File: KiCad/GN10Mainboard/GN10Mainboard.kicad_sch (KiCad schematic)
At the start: 130 parts, among them J1 USB_C_Receptacle_USB2.0_16P, J10 Conn_01x02_Pin, J2 Conn_01x04, J3 Conn_01x04, J4 USB_C_Receptacle_USB2.0_16P, J5 Conn_01x04, J6 Conn_01x06, J7 Conn_01x04, J8 Conn_01x04, J9 XT30PW-M, SW1 SW_DIP_x04, SW2 SW_Push, SW4 SW_Push, SW5 SW_Push, U1 STM32G474RCTx, U10 3.3V, U2 FT231XS, U3 RNBD451, U4 FT231XS, U5 MCP2562-E-SN, U6 MCP2562-E-SN, U7 BNO055, U8 7segmentLED, U9 OKL-T/x-W5N-C, Y1 32.768kHz, Y2 24MHz, Y3 Crystal

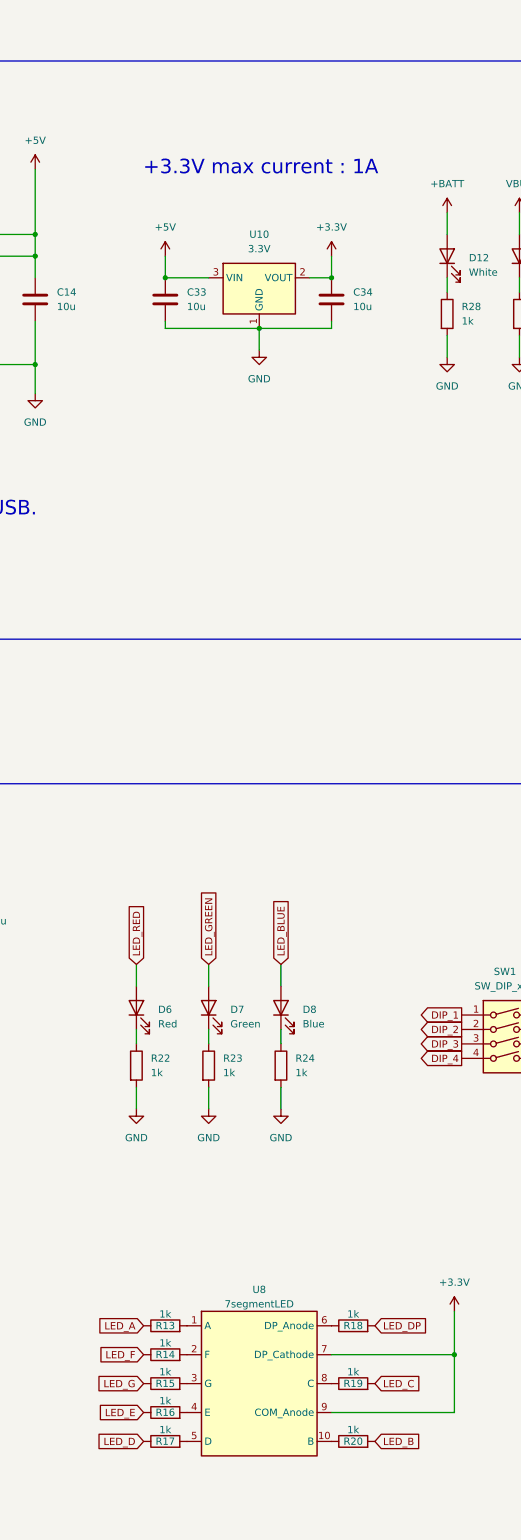
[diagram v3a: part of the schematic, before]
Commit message: Added a reverse voltage protection diode to the linear regulator and fixed the 7seg LED because its resistance was too high.
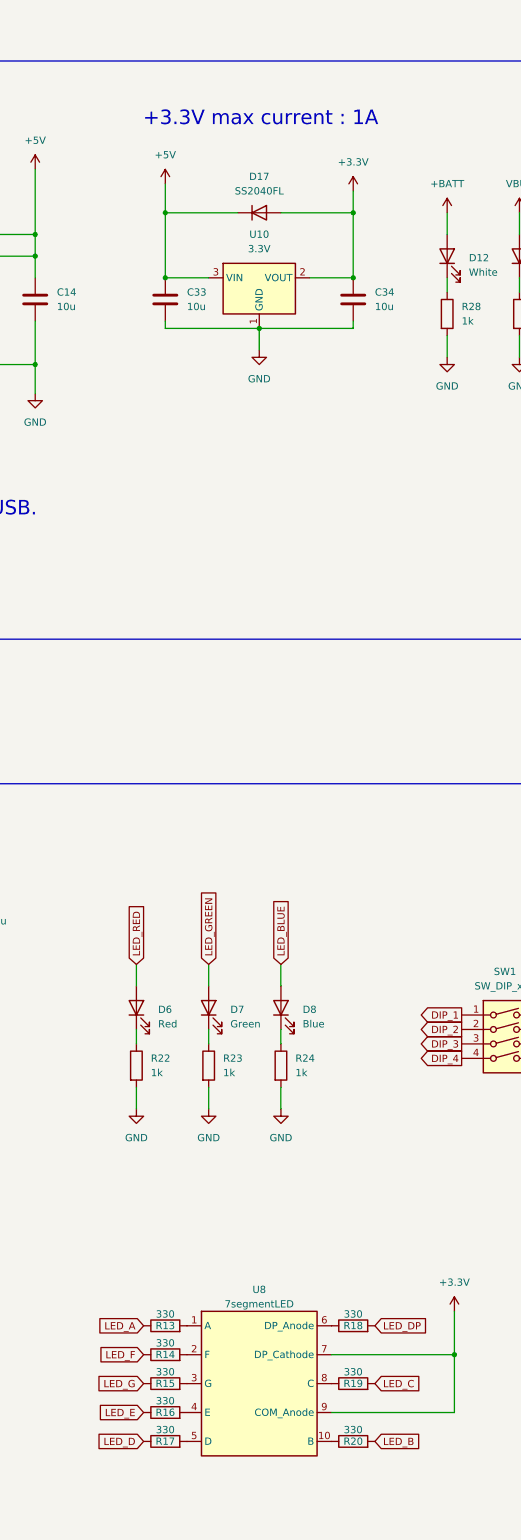
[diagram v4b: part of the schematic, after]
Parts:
- added D17: SS2040FL, symbol Device:D
- R13, R14, R15, R16, R17, R18, R19, R20: value 1k -> 330
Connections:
- net +3.3V: now also D17.2 (A)
- net +5V: now also D17.1 (K)
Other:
- moved on the sheet: C34
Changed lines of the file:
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@@
 	)
 	(junction
-		(at 203.2 63.5)
+		(at 207.01 63.5)
 		(diameter 0)
 		(color 0 0 0 0)
@@
 	)
 	(junction
+		(at 173.99 52.07)
+		(diameter 0)
+		(color 0 0 0 0)
+	)
+	(junction
 		(at 118.11 179.07)
 		(diameter 0)
@@
 		(color 0 0 0 0)
 	)
+	(junction
+		(at 207.01 52.07)
+		(diameter 0)
+		(color 0 0 0 0)
+	)
 	(no_connect
 		(at 431.8 77.47)
@@
 	(wire
 		(pts
-			(xy 203.2 71.12) (xy 203.2 72.39)
+			(xy 207.01 71.12) (xy 207.01 72.39)
 		)
 		(stroke
@@
 	(wire
 		(pts
+			(xy 173.99 52.07) (xy 186.69 52.07)
+		)
+		(stroke
+			(width 0)
+			(type default)
+		)
+	)
+	(wire
+		(pts
 			(xy 81.28 367.03) (xy 95.25 367.03)
 		)
@@
 	(wire
 		(pts
-			(xy 199.39 63.5) (xy 203.2 63.5)
+			(xy 199.39 63.5) (xy 207.01 63.5)
 		)
 		(stroke
@@
 	(wire
 		(pts
-			(xy 173.99 59.69) (xy 173.99 63.5)
+			(xy 173.99 46.99) (xy 173.99 52.07)
 		)
 		(stroke
@@
 	(wire
 		(pts
+			(xy 173.99 52.07) (xy 173.99 63.5)
+		)
+		(stroke
+			(width 0)
+			(type default)
+		)
+	)
+	(wire
+		(pts
 			(xy 455.93 82.55) (xy 448.31 82.55)
 		)
@@
 	(wire
 		(pts
+			(xy 194.31 52.07) (xy 207.01 52.07)
+		)
+		(stroke
+			(width 0)
+			(type default)
+		)
+	)
+	(wire
+		(pts
 			(xy 67.31 198.12) (xy 67.31 200.66)
 		)
@@
 	(wire
 		(pts
+			(xy 207.01 52.07) (xy 207.01 63.5)
+		)
+		(stroke
+			(width 0)
+			(type default)
+		)
+	)
+	(wire
+		(pts
 			(xy 345.44 377.19) (xy 358.14 377.19)
 		)
@@
 	(wire
 		(pts
-			(xy 203.2 72.39) (xy 190.5 72.39)
+			(xy 207.01 72.39) (xy 190.5 72.39)
 		)
 		(stroke
@@
 	(wire
 		(pts
-			(xy 203.2 59.69) (xy 203.2 63.5)
+			(xy 207.01 48.26) (xy 207.01 52.07)
 		)
 		(stroke
@@
 	(text "+3.3V max current : 1A"
 		(exclude_from_sim no)
-		(at 190.754 44.196 0)
+		(at 190.754 35.56 0)
 		(effects
 			(font
@@
 			)
 		)
-		(property "Value" "1k"
+		(property "Value" "330"
 			(at 207.01 265.938 90)
 			(effects
@@
 			)
 		)
-		(property "Value" "1k"
+		(property "Value" "330"
 			(at 173.99 245.618 90)
 			(effects
@@
 			)
 		)
-		(property "Value" "1k"
+		(property "Value" "330"
 			(at 173.99 250.698 90)
 			(effects
@@
 			)
 		)
-		(property "Value" "1k"
+		(property "Value" "330"
 			(at 173.99 265.938 90)
 			(effects
@@
 			)
 		)
-		(property "Value" "1k"
+		(property "Value" "330"
 			(at 173.99 255.778 90)
 			(effects
@@
 			)
 		)
-		(property "Value" "1k"
+		(property "Value" "330"
 			(at 207.01 245.618 90)
 			(effects
@@
 	(symbol
 		(lib_id "Device:C")
-		(at 203.2 67.31 0)
+		(at 207.01 67.31 0)
 		(unit 1)
 		(exclude_from_sim no)
@@
 		(fields_autoplaced yes)
 		(property "Reference" "C34"
-			(at 207.01 66.0399 0)
+			(at 210.82 66.0399 0)
 			(effects
 				(font
@@
 		)
 		(property "Value" "10u"
-			(at 207.01 68.5799 0)
+			(at 210.82 68.5799 0)
 			(effects
 				(font
@@
 		)
 		(property "Footprint" ""
-			(at 204.1652 71.12 0)
+			(at 207.9752 71.12 0)
 			(effects
 				(font
@@
 		)
 		(property "Datasheet" "~"
-			(at 203.2 67.31 0)
+			(at 207.01 67.31 0)
 			(effects
 				(font
@@
 		)
 		(property "Description" "Unpolarized capacitor"
-			(at 203.2 67.31 0)
+			(at 207.01 67.31 0)
 			(effects
 				(font
@@
 			)
 		)
-		(property "Value" "1k"
+		(property "Value" "330"
 			(at 173.99 260.858 90)
 			(effects
@@
 	)
 	(symbol
+		(lib_id "Device:D")
+		(at 190.5 52.07 0)
+		(unit 1)
+		(exclude_from_sim no)
+		(in_bom yes)
+		(on_board yes)
+		(dnp no)
+		(fields_autoplaced yes)
+		(property "Reference" "D17"
+			(at 190.5 45.72 0)
+			(effects
+				(font
+					(size 1.27 1.27)
+				)
+			)
+		)
+		(property "Value" "SS2040FL"
+			(at 190.5 48.26 0)
+			(effects
+				(font
+					(size 1.27 1.27)
+				)
+			)
+		)
+		(property "Footprint" ""
+			(at 190.5 52.07 0)
+			(effects
+				(font
+					(size 1.27 1.27)
+				)
+				(hide yes)
+			)
+		)
+		(property "Datasheet" "~"
+			(at 190.5 52.07 0)
+			(effects
+				(font
+					(size 1.27 1.27)
+				)
+				(hide yes)
+			)
+		)
+		(property "Description" "Diode"
+			(at 190.5 52.07 0)
+			(effects
+				(font
+					(size 1.27 1.27)
+				)
+				(hide yes)
+			)
+		)
+		(property "Sim.Device" "D"
+			(at 190.5 52.07 0)
+			(effects
+				(font
+					(size 1.27 1.27)
+				)
+				(hide yes)
+			)
+		)
+		(property "Sim.Pins" "1=K 2=A"
+			(at 190.5 52.07 0)
+			(effects
+				(font
+					(size 1.27 1.27)
+				)
+				(hide yes)
+			)
+		)
+		(pin "1"
+		)
+		(pin "2"
+		)
+		(instances
+			(project ""
+				(path "/b58ae320-37f1-47e7-bf16-145390e42e75"
+					(reference "D17")
+					(unit 1)
+				)
+			)
+		)
+	)
+	(symbol
 		(lib_id "power:GND")
 		(at 142.24 242.57 0)
@@
 	(symbol
 		(lib_id "power:+3.3V")
-		(at 203.2 59.69 0)
+		(at 207.01 48.26 0)
 		(unit 1)
 		(exclude_from_sim no)
@@
 		(fields_autoplaced yes)
 		(property "Reference" "#PWR069"
-			(at 203.2 63.5 0)
+			(at 207.01 52.07 0)
 			(effects
 				(font
@@
 		)
 		(property "Value" "+3.3V"
-			(at 203.2 54.61 0)
+			(at 207.01 43.18 0)
 			(effects
 				(font
@@
 		)
 		(property "Footprint" ""
-			(at 203.2 59.69 0)
+			(at 207.01 48.26 0)
 			(effects
 				(font
@@
 		)
 		(property "Datasheet" ""
-			(at 203.2 59.69 0)
+			(at 207.01 48.26 0)
 			(effects
 				(font
@@
 		)
 		(property "Description" "Power symbol creates a global label with name \"+3.3V\""
-			(at 203.2 59.69 0)
+			(at 207.01 48.26 0)
 			(effects
 				(font
@@
 	(symbol
 		(lib_id "power:+5V")
-		(at 173.99 59.69 0)
+		(at 173.99 46.99 0)
 		(unit 1)
 		(exclude_from_sim no)
@@
 		(fields_autoplaced yes)
 		(property "Reference" "#PWR067"
-			(at 173.99 63.5 0)
+			(at 173.99 50.8 0)
 			(effects
 				(font
@@
 		)
 		(property "Value" "+5V"
-			(at 173.99 54.61 0)
+			(at 173.99 41.91 0)
 			(effects
 				(font
@@
 		)
 		(property "Footprint" ""
-			(at 173.99 59.69 0)
+			(at 173.99 46.99 0)
 			(effects
 				(font
@@
 		)
 		(property "Datasheet" ""
-			(at 173.99 59.69 0)
+			(at 173.99 46.99 0)
 			(effects
 				(font
@@
 		)
 		(property "Description" "Power symbol creates a global label with name \"+5V\""
-			(at 173.99 59.69 0)
+			(at 173.99 46.99 0)
 			(effects
 				(font
@@
 			)
 		)
-		(property "Value" "1k"
+		(property "Value" "330"
 			(at 207.01 255.778 90)
 			(effects

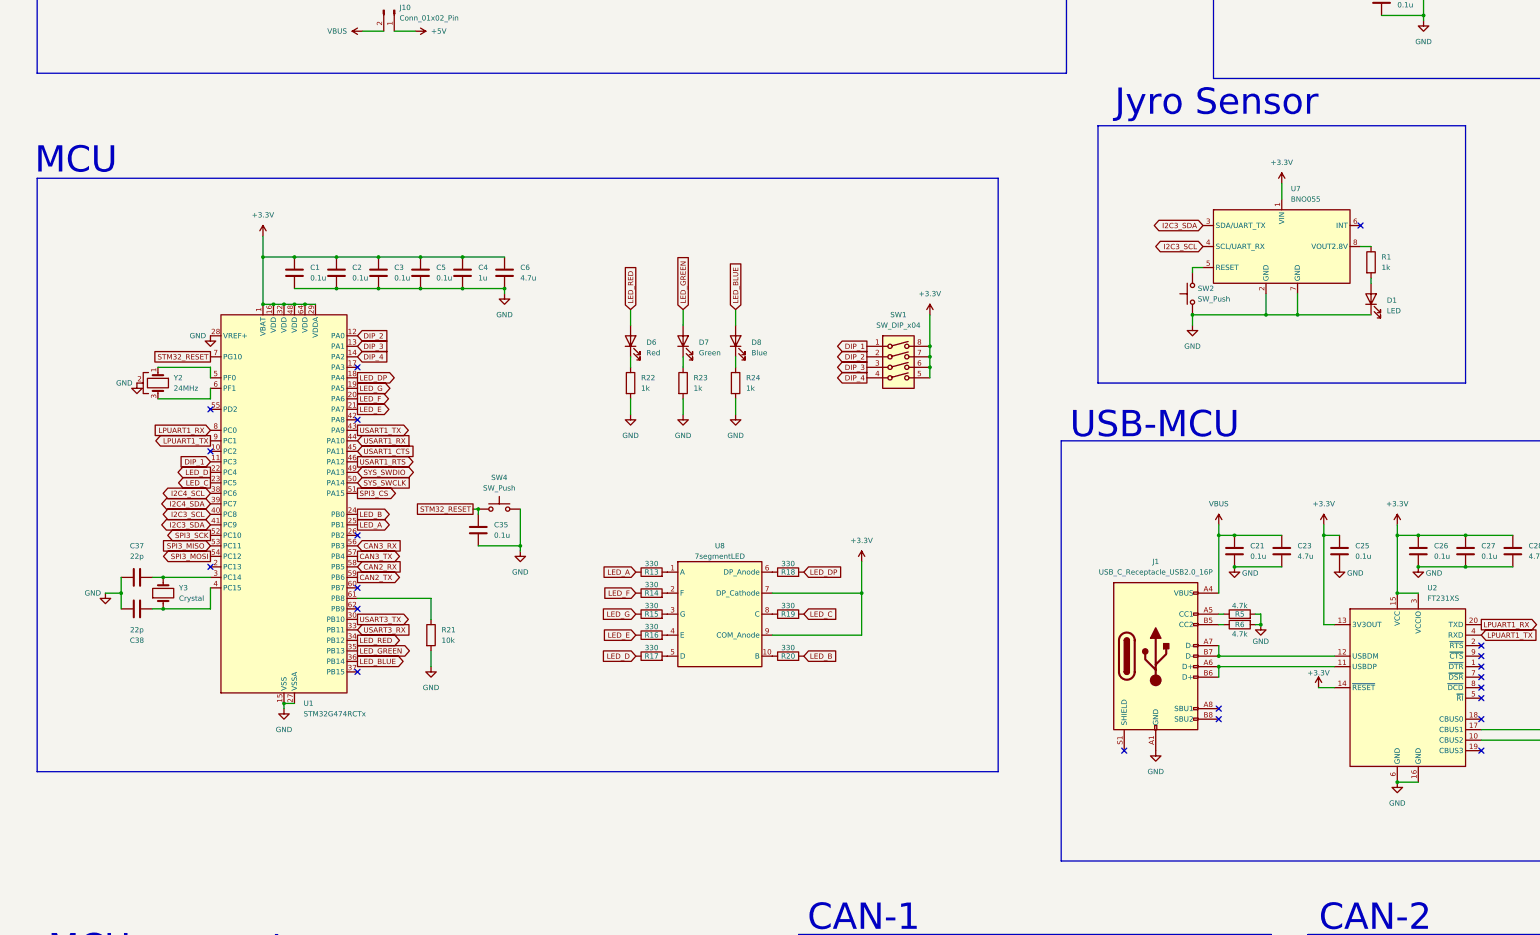
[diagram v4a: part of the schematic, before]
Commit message: add: transistor array for drive a 7 segment LED.
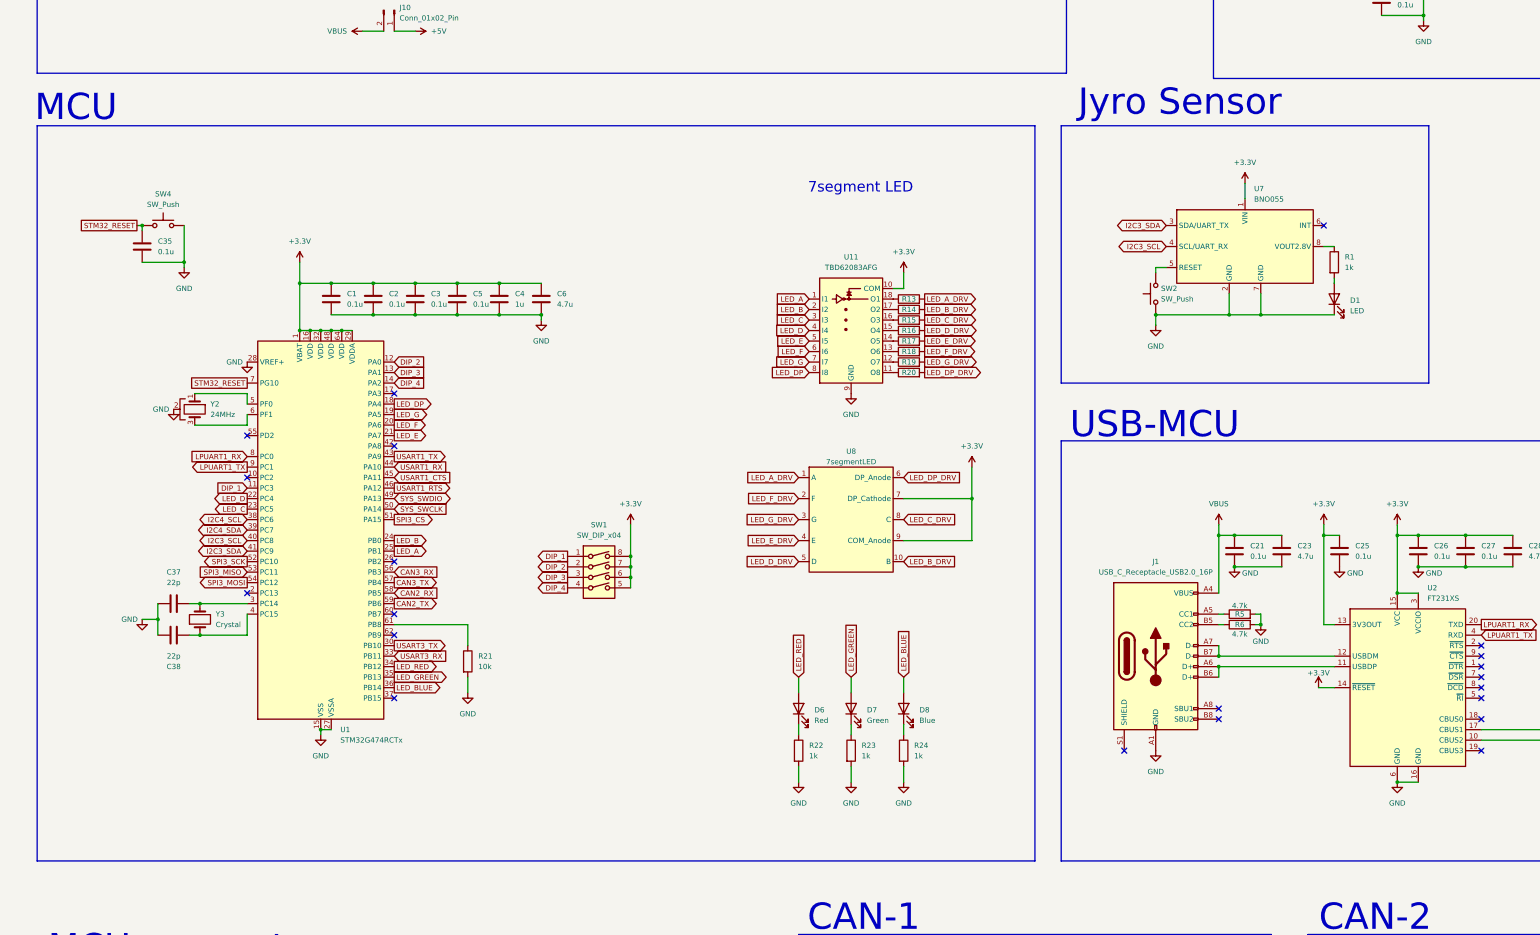
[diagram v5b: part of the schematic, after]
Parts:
- added U11: TBD62083AFG, symbol Transistor_Array:ULN2803A
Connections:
- net +3.3V: now also U11.10 (COM)
- net GND: now also U11.9 (GND)
- net LED_A: now also U11.1 (I1); no longer R13.1
- net LED_B: now also U11.2 (I2); no longer R20.2
- net LED_C: now also U11.3 (I3); no longer R19.2
- net LED_D: now also U11.4 (I4); no longer R17.1
- net LED_DP: now also U11.8 (I8); no longer R18.2
- net LED_E: now also U11.5 (I5); no longer R16.1
- net LED_F: now also U11.6 (I6); no longer R14.1
- net LED_G: now also U11.7 (I7); no longer R15.1
- net at R20.1: now also U11.11 (O8); no longer U8.10 (B)
- net LED_A_DRV: now reaches R13.2, U8.1 (A)
- net LED_B_DRV: now reaches R14.2
- net LED_B_DRV: now also U8.10 (B); no longer U8.2 (F)
- net LED_D_DRV: now reaches U8.5 (D)
- net LED_D_DRV: now also R16.2; no longer R17.2
- net LED_C_DRV: now reaches R15.2
- net LED_C_DRV: now also U8.8 (C); no longer U8.3 (G)
- net at R18.1: now also U11.13 (O6); no longer U8.6 (DP_Anode)
- net LED_E_DRV: now reaches U8.4 (E)
- net LED_E_DRV: now also R17.2; no longer R16.2
- net at R19.1: now also U11.12 (O7); no longer U8.8 (C)
- new net: R14.1, U11.17 (O2)
- new net: R13.1, U11.18 (O1)
- new net: R15.1, U11.16 (O3)
- new net: R17.1, U11.14 (O5)
- new net: R16.1, U11.15 (O4)
- new net LED_DP_DRV: R20.2, U8.6 (DP_Anode)
- new net LED_F_DRV: R18.2, U8.2 (F)
- new net LED_G_DRV: R19.2, U8.3 (G)
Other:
- note added: "7segment LED"
- moved on the sheet: C1, C2, C3, C35, C37, C38, C4, C5, C6, D1, D6, D7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

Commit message: change from FT231XS to FT2232HQ
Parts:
- removed C21, C22, C25, C26, C27, C29, C30, C31: 0.1u, symbol Device:C
- removed C23, C24, C28, C32: 4.7u, symbol Device:C
- removed D2, D4: Green, symbol Device:LED
- removed D3, D5: Blue, symbol Device:LED
- removed J1, J4: USB_C_Receptacle_USB2.0_16P, Connector_USB:USB_C_Receptacle_HRO_TYPE-C-31-M-12, symbol Connector:USB_C_Receptacle_USB2.0_16P
- removed JP13, JP14: Jumper_2_Open, symbol Jumper:Jumper_2_Open
- removed JP4, JP6, JP7, JP8: SolderJumper_2_Open, Jumper:SolderJumper-2_P1.3mm_Open_RoundedPad1.0x1.5mm, symbol Jumper:SolderJumper_2_Open
- removed R10, R11, R12, R9: 470, symbol Device:R
- removed R5, R6, R7, R8: 4.7k, symbol Device:R
- removed U2, U4: FT231XS, Package_SO:SSOP-20_3.9x8.7mm_P0.635mm, symbol Interface_USB:FT231XS
- added C39, C43: 1u, symbol Device:C
- added C40, C41, C42, C44, C45, C48, C49: 0.1u, symbol Device:C
- added C46, C47: 10u, symbol Device:C
- added C50: C, symbol Device:C
- added C51: 0.1u, Resistor_SMD:R_0603_1608Metric_Pad0.98x0.95mm_HandSolder, symbol Device:C
- added C52: 4.7u, Resistor_SMD:R_0603_1608Metric_Pad0.98x0.95mm_HandSolder, symbol Device:C
- added D18, D20: Green, LED_SMD:LED_0603_1608Metric_Pad1.05x0.95mm_HandSolder, symbol Device:LED
- added D19, D21: Blue, LED_SMD:LED_0603_1608Metric_Pad1.05x0.95mm_HandSolder, symbol Device:LED
- added J11: USB_C_Receptacle_USB2.0_16P, Connector_USB:USB_C_Receptacle_HRO_TYPE-C-31-M-12, symbol Connector:USB_C_Receptacle_USB2.0_16P
- added JP13, JP15: SolderJumper_2_Open, Jumper:SolderJumper-2_P1.3mm_Open_RoundedPad1.0x1.5mm, symbol Jumper:SolderJumper_2_Open
- added L1, L2: L, symbol Device:L
- added R34, R35, R36, R37: 470, Resistor_SMD:R_0603_1608Metric_Pad0.98x0.95mm_HandSolder, symbol Device:R
- added R38, R39: 4.7k, Resistor_SMD:R_0603_1608Metric_Pad0.98x0.95mm_HandSolder, symbol Device:R
- added R40: 12k, symbol Device:R
- added R41: 1k, symbol Device:R
- added U12: FT2232HQ, Package_DFN_QFN:QFN-64-1EP_9x9mm_P0.5mm_EP4.35x4.35mm, symbol Interface_USB:FT2232HQ
- added Y4: Crystal_GND2, symbol Device:Crystal_GND2
- C1, C10, C17, C18, C2, C3, C35, C36, C4, C5, C6, C7, C8, C9, R1, R13, R14, R15, R16, R17, R18, R19, R2, R20, R21, R22, R23, R24, R25, R26, R27, R28, R29, R3, R31, R32, R33, R4: footprint (none) -> Resistor_SMD:R_0603_1608Metric_Pad0.98x0.95mm_HandSolder
- C11: footprint (none) -> Capacitor_THT:C_Radial_D6.3mm_H11.0mm_P2.50mm
- C12: footprint (none) -> Capacitor_THT:C_Rect_L11.0mm_W6.3mm_P10.00mm_MKT
- C15, C16, C37, C38: footprint (none) -> Capacitor_SMD:C_0402_1005Metric_Pad0.74x0.62mm_HandSolder
- C19, C20, C33, C34: footprint (none) -> Capacitor_SMD:C_0805_2012Metric_Pad1.18x1.45mm_HandSolder
- D1: value LED -> Blue; footprint (none) -> LED_SMD:LED_0603_1608Metric_Pad1.05x0.95mm_HandSolder
- D10, D11, D12, D13, D14, D15, D16, D6, D7, D8, D9: footprint (none) -> LED_SMD:LED_0603_1608Metric_Pad1.05x0.95mm_HandSolder
- D17: footprint (none) -> Diode_SMD:Nexperia_CFP3_SOD-123W
- J10: footprint (none) -> Connector_PinHeader_2.54mm:PinHeader_1x02_P2.54mm_Vertical
- J6: footprint (none) -> Connector_JST:JST_XH_B6B-XH-A_1x06_P2.50mm_Vertical
- R30: value R -> 10k; footprint (none) -> Resistor_SMD:R_0603_1608Metric_Pad0.98x0.95mm_HandSolder
- SW2, SW4, SW5: footprint (none) -> GN10_Parts:TVAF
- TP1, TP2: footprint (none) -> TestPoint:TestPoint_Pad_1.5x1.5mm
- U11: footprint (none) -> Package_SO:SOP-18_7x12.5mm_P1.27mm
- Y1, Y3: footprint (none) -> Crystal:Crystal_SMD_3215-2Pin_3.2x1.5mm
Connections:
- net +3.3V: now also C39.1, C40.1, C41.1, C42.1, L1.1, L2.1, R34.1, R35.1, R36.1, R37.1, R41.1, U12.20 (VCCIO), U12.31 (VCCIO), U12.42 (VCCIO), U12.50 (VREGIN), U12.56 (VCCIO)
- net BLE_UART_MODE: now also JP13.2 (B)
- net GND: now also C39.2, C40.2, C41.2, C42.2, C43.2, C44.2, C45.2, C46.2, C47.2, C48.2, C49.2, C50.2, C51.2, C52.2, J11.A1 (GND), J11.A12 (GND), J11.B1 (GND), J11.B12 (GND), JP13.1 (A), JP15.1 (A), R38.2, R39.2, R40.2, U12.1 (GND), U12.10 (AGND), U12.11 (GND), U12.13 (TEST), U12.15 (GND), U12.25 (GND), U12.35 (GND), U12.36 (~{SUSPEND}), U12.47 (GND), U12.5 (GND), U12.51 (GND), U12.60 (~{PWREN}), U12.65 (GND), Y4.2
- net LPUART1_RX: now also U12.16 (ADBUS0)
- net LPUART1_TX: now also U12.17 (ADBUS1)
- net SERIAL_CTS: now also U12.43 (BDBUS4)
- net SERIAL_RTS: now also U12.40 (BDBUS2)
- net SERIAL_RX: now also U12.39 (BDBUS1)
- net SERIAL_TX: now also U12.38 (BDBUS0)
- net VBUS: now also C51.1, C52.1, J11.A4 (VBUS), J11.A9 (VBUS), J11.B4 (VBUS), J11.B9 (VBUS)
- net at R2.2, U9.1 (ON/OFF): now also JP15.2 (B)
- new net: D21.1 (K), U12.55 (BCBUS4)
- new net: D21.2 (A), R37.2
- new net: D20.2 (A), R36.2
- new net: J11.A5 (CC1), R38.1
- new net: R41.2, U12.14 (~{RESET})
- new net: U12.2 (OSCI), Y4.1
- new net: U12.3 (OSCO), Y4.3
- new net: R40.1, U12.6 (REF)
- new net: D18.2 (A), R34.2
- new net: D19.1 (K), U12.30 (ACBUS4)
- new net: D19.2 (A), R35.2
- new net: C46.1, C48.1, L1.2, U12.9 (VPLL)
- new net: C47.1, C49.1, L2.2, U12.4 (VPHY)
- new net: D18.1 (K), U12.29 (ACBUS3)
- new net: D20.1 (K), U12.54 (BCBUS3)
- new net: J11.A7 (D-), J11.B7 (D-), U12.7 (DM)
- new net: J11.A6 (D+), J11.B6 (D+), U12.8 (DP)
- new net: J11.B5 (CC2), R39.1
- new net +1V8: C43.1, C44.1, C45.1, C50.1, U12.12 (VCORE), U12.37 (VCORE), U12.49 (VREGOUT), U12.64 (VCORE)
- no-connect marks 47 -> 55
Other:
- note added: "USB"
- note removed: "USB-BLEmodule/MCU"
- note removed: "USB-MCU"
- moved on the sheet: C1, C10, C11, C12, C13, C14, C15, C16, C17, C18, C19, C2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

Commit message: update: pdf and anotation
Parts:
- renumbered C13 to C1, C3 to C10, C5 to C11, C4 to C12, C6 to C13, C20 to C14, C17 to C15, C15 to C16, C36 to C17, C16 to C18, C18 to C19, C14 to C2, C19 to C20, C51 to C21, C52 to C22, C50 to C23, C46 to C24, C47 to C25, C48 to C26, C49 to C27, C43 to C28, C44 to C29, C33 to C3, C39 to C30, C45 to C31, C40 to C32, C41 to C33, C42 to C34, C9 to C35, C7 to C36, C10 to C37, C8 to C38, C12 to C39, C34 to C4, C11 to C40, C35 to C5, C37 to C6, C38 to C7, C1 to C8, C2 to C9, D17 to D1, D14 to D10, D15 to D11, D16 to D12, D18 to D13, D20 to D14, D19 to D15, D21 to D16, D1 to D17, D12 to D2, D11 to D3, D10 to D4, D9 to D5, D13 to D9, J9 to J1, J10 to J2, J11 to J3, J3 to J4, J2 to J5, J8 to J6, J5 to J8, J6 to J9, JP15 to JP1, JP3 to JP10, JP13 to JP2, JP9 to JP3, JP10 to JP4, JP11 to JP5, JP12 to JP6, JP5 to JP7, JP1 to JP8, JP2 to JP9, R2 to R1, R23 to R10, R24 to R11, R13 to R12, R14 to R13, R15 to R14, R16 to R15, R17 to R16, R18 to R17, R19 to R18, R20 to R19, R3 to R2, R30 to R20, R29 to R21, R31 to R22, R32 to R23, R33 to R24, R38 to R25, R39 to R26, R41 to R27, R40 to R28, R34 to R29, R4 to R3, R36 to R30, R35 to R31, R37 to R32, R1 to R33, R28 to R4, R27 to R5, R26 to R6, R25 to R7, R21 to R8, R22 to R9, SW4 to SW1, SW1 to SW2, SW5 to SW3, SW2 to SW4, U9 to U1, U7 to U10, U10 to U2, U1 to U3, U11 to U4, U8 to U5, U3 to U6, U12 to U7, U6 to U8, U5 to U9, Y2 to Y1, Y3 to Y2, Y1 to Y3
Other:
- moved on the sheet: C14, C15, C16, C17, C18, C19, C20, C21, C22, C23, C24, C25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
